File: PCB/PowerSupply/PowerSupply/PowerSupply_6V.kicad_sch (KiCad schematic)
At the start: 18 parts

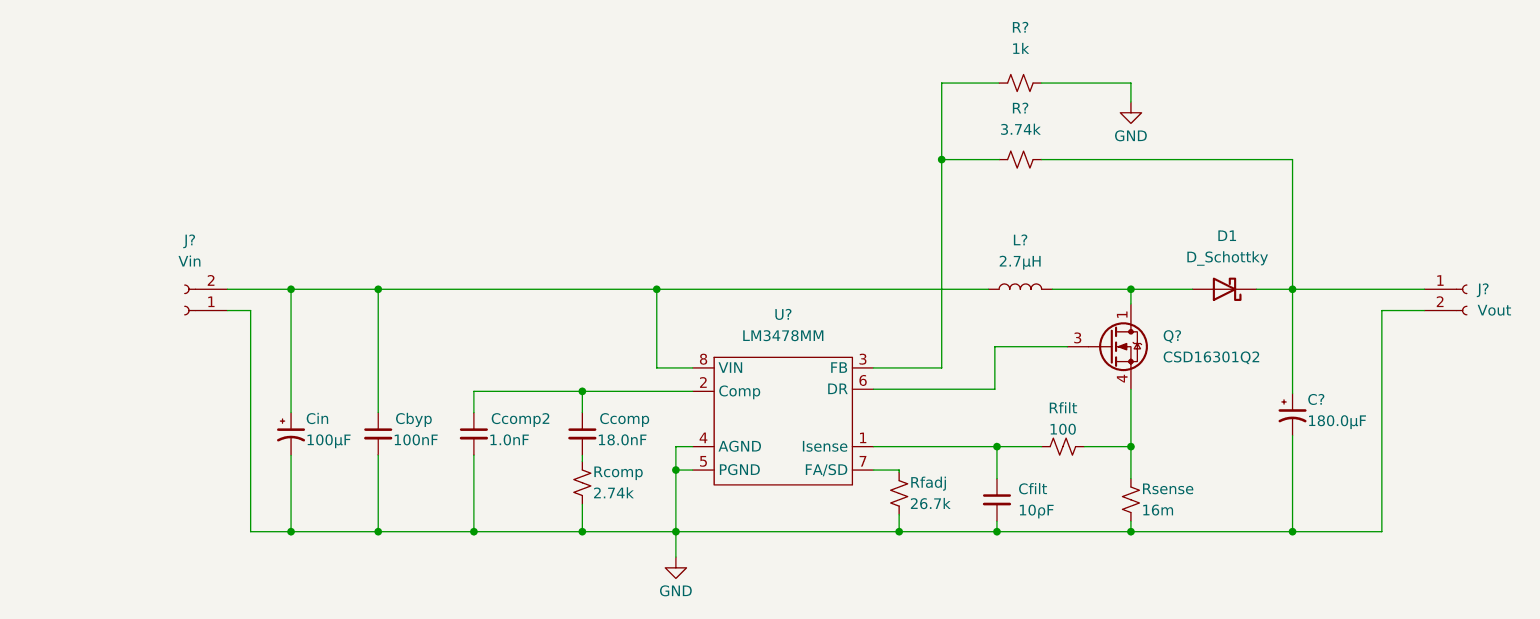
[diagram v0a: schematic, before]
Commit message: Finalized both power supply
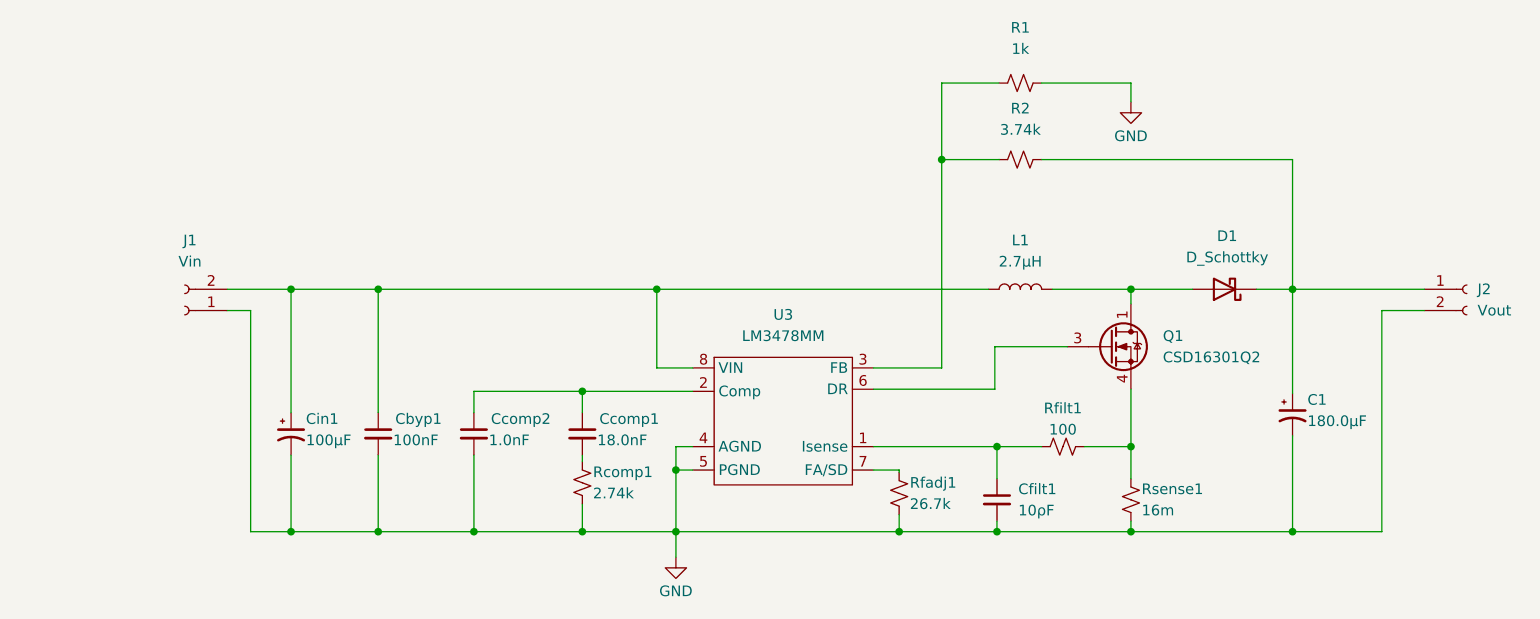
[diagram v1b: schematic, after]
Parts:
- gave numbers to parts that had none: 8
- renumbered Cbyp to Cbyp1, Ccomp to Ccomp1, Cfilt to Cfilt1, Cin to Cin1, Rcomp to Rcomp1, Rfadj to Rfadj1, Rfilt to Rfilt1, Rsense to Rsense1
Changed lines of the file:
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@@
   (symbol (lib_id "Device:L") (at 155.194 87.63 90) (unit 1)
     (in_bom yes) (on_board yes)
-    (property "Reference" "L?" (id 0) (at 155.194 81.788 90))
+    (property "Reference" "L1" (id 0) (at 155.194 81.788 90))
     (property "Value" "2.7µH" (id 1) (at 155.194 84.328 90))
     (property "Footprint" "Inductor_SMD:L_TDK_VLP8040" (id 2) (at 155.194 87.63 0)
@@
   (symbol (lib_id "Connector:Conn_01x02_Female") (at 55.372 90.17 180) (unit 1)
     (in_bom yes) (on_board yes) (fields_autoplaced)
-    (property "Reference" "J?" (id 0) (at 56.007 81.788 0))
+    (property "Reference" "J1" (id 0) (at 56.007 81.788 0))
     (property "Value" "Vin" (id 1) (at 56.007 84.328 0))
     (property "Footprint" "Connector_PinHeader_2.54mm:PinHeader_1x02_P2.54mm_Vertical" (id 2) (at 55.372 90.17 0)
@@
   (symbol (lib_id "Transistor_FET:CSD16301Q2") (at 165.862 94.488 0) (unit 1)
     (in_bom yes) (on_board yes) (fields_autoplaced)
-    (property "Reference" "Q?" (id 0) (at 172.212 93.2179 0)
+    (property "Reference" "Q1" (id 0) (at 172.212 93.2179 0)
       (effects (font (size 1.27 1.27)) (justify left))
     )
@@
   (symbol (lib_id "Device:C_Polarized_Small_US") (at 187.706 102.616 0) (unit 1)
     (in_bom yes) (on_board yes)
-    (property "Reference" "C?" (id 0) (at 189.484 100.838 0)
+    (property "Reference" "C1" (id 0) (at 189.484 100.838 0)
       (effects (font (size 1.27 1.27)) (justify left))
     )
@@
   (symbol (lib_id "Connector:Conn_01x02_Female") (at 208.534 87.63 0) (unit 1)
     (in_bom yes) (on_board yes) (fields_autoplaced)
-    (property "Reference" "J?" (id 0) (at 209.804 87.6299 0)
+    (property "Reference" "J2" (id 0) (at 209.804 87.6299 0)
       (effects (font (size 1.27 1.27)) (justify left))
     )
@@
   (symbol (lib_id "Device:R_Small_US") (at 155.194 72.136 90) (unit 1)
     (in_bom yes) (on_board yes) (fields_autoplaced)
-    (property "Reference" "R?" (id 0) (at 155.194 66.04 90))
+    (property "Reference" "R2" (id 0) (at 155.194 66.04 90))
     (property "Value" "3.74k" (id 1) (at 155.194 68.58 90))
     (property "Footprint" "Resistor_SMD:R_0402_1005Metric_Pad0.72x0.64mm_HandSolder" (id 2) (at 155.194 72.136 0)
@@
   (symbol (lib_id "Device:C_Polarized_Small_US") (at 68.072 104.902 0) (unit 1)
     (in_bom yes) (on_board yes)
-    (property "Reference" "Cin" (id 0) (at 69.85 103.124 0)
+    (property "Reference" "Cin1" (id 0) (at 69.85 103.124 0)
       (effects (font (size 1.27 1.27)) (justify left))
     )
@@
   (symbol (lib_id "Device:R_Small_US") (at 140.716 112.014 0) (unit 1)
     (in_bom yes) (on_board yes)
-    (property "Reference" "Rfadj" (id 0) (at 141.986 110.744 0)
+    (property "Reference" "Rfadj1" (id 0) (at 141.986 110.744 0)
       (effects (font (size 1.27 1.27)) (justify left))
     )
@@
   (symbol (lib_id "CustomPower:LM3478MM") (at 126.238 90.678 0) (unit 1)
     (in_bom yes) (on_board yes) (fields_autoplaced)
-    (property "Reference" "U?" (id 0) (at 126.873 90.678 0))
+    (property "Reference" "U3" (id 0) (at 126.873 90.678 0))
     (property "Value" "LM3478MM" (id 1) (at 126.873 93.218 0))
     (property "Footprint" "Package_SO:SOIC-8-1EP_3.9x4.9mm_P1.27mm_EP2.29x3mm" (id 2) (at 126.238 90.678 0)
@@
   (symbol (lib_id "Device:C_Small") (at 152.4 112.776 0) (unit 1)
     (in_bom yes) (on_board yes) (fields_autoplaced)
-    (property "Reference" "Cfilt" (id 0) (at 154.94 111.5122 0)
+    (property "Reference" "Cfilt1" (id 0) (at 154.94 111.5122 0)
       (effects (font (size 1.27 1.27)) (justify left))
     )
@@
   (symbol (lib_id "Device:R_Small_US") (at 155.194 62.992 90) (unit 1)
     (in_bom yes) (on_board yes) (fields_autoplaced)
-    (property "Reference" "R?" (id 0) (at 155.194 56.388 90))
+    (property "Reference" "R1" (id 0) (at 155.194 56.388 90))
     (property "Value" "1k" (id 1) (at 155.194 58.928 90))
     (property "Footprint" "Resistor_SMD:R_0402_1005Metric_Pad0.72x0.64mm_HandSolder" (id 2) (at 155.194 62.992 0)
@@
   (symbol (lib_id "power:GND") (at 114.046 119.634 0) (unit 1)
     (in_bom yes) (on_board yes)
-    (property "Reference" "#PWR?" (id 0) (at 114.046 125.984 0)
+    (property "Reference" "#PWR0101" (id 0) (at 114.046 125.984 0)
       (effects (font (size 1.27 1.27)) hide)
     )
@@
   (symbol (lib_id "Device:R_Small_US") (at 102.87 110.744 0) (unit 1)
     (in_bom yes) (on_board yes)
-    (property "Reference" "Rcomp" (id 0) (at 104.14 109.474 0)
+    (property "Reference" "Rcomp1" (id 0) (at 104.14 109.474 0)
       (effects (font (size 1.27 1.27)) (justify left))
     )
@@
   (symbol (lib_id "Device:C_Small") (at 78.486 104.902 0) (unit 1)
     (in_bom yes) (on_board yes)
-    (property "Reference" "Cbyp" (id 0) (at 80.518 103.124 0)
+    (property "Reference" "Cbyp1" (id 0) (at 80.518 103.124 0)
       (effects (font (size 1.27 1.27)) (justify left))
     )
@@
   (symbol (lib_id "Device:C_Small") (at 102.87 104.902 0) (unit 1)
     (in_bom yes) (on_board yes)
-    (property "Reference" "Ccomp" (id 0) (at 104.902 103.124 0)
+    (property "Reference" "Ccomp1" (id 0) (at 104.902 103.124 0)
       (effects (font (size 1.27 1.27)) (justify left))
     )
@@
   (symbol (lib_id "Device:R_Small_US") (at 160.274 106.426 90) (unit 1)
     (in_bom yes) (on_board yes)
-    (property "Reference" "Rfilt" (id 0) (at 160.274 101.854 90))
+    (property "Reference" "Rfilt1" (id 0) (at 160.274 101.854 90))
     (property "Value" "100" (id 1) (at 160.274 104.394 90))
     (property "Footprint" "Resistor_SMD:R_0805_2012Metric_Pad1.20x1.40mm_HandSolder" (id 2) (at 160.274 106.426 0)
@@
   (symbol (lib_id "Device:R_Small_US") (at 168.402 112.776 0) (unit 1)
     (in_bom yes) (on_board yes)
-    (property "Reference" "Rsense" (id 0) (at 169.672 111.506 0)
+    (property "Reference" "Rsense1" (id 0) (at 169.672 111.506 0)
       (effects (font (size 1.27 1.27)) (justify left))
     )
@@
   (symbol (lib_id "power:GND") (at 168.402 65.278 0) (unit 1)
     (in_bom yes) (on_board yes)
-    (property "Reference" "#PWR?" (id 0) (at 168.402 71.628 0)
-      (effects (font (size 1.27 1.27)) hide)
-    )
+    (property "Reference" "#PWR0102" (id 0) (at 168.402 71.628 0)
+      (effects (font (size 1.27 1.27)) hide)
+    )

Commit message: Fixed Zach's errors :/ smh
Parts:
- added J6: Vout, Connector_PinHeader_2.54mm:PinHeader_1x02_P2.54mm_Vertical, symbol Connector:Conn_01x02_Female
- Cbyp1: footprint Capacitor_SMD:C_0402_1005Metric_Pad0.74x0.62mm_HandSolder -> Capacitor_SMD:C_0805_2012Metric_Pad1.18x1.45mm_HandSolder
- Ccomp1, R1, R2, Rfadj1: footprint Resistor_SMD:R_0402_1005Metric_Pad0.72x0.64mm_HandSolder -> Resistor_SMD:R_0805_2012Metric_Pad1.20x1.40mm_HandSolder
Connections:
- net GND: now also J6.2 (Pin_2)
- net at C1.1, D1.1 (K), J2.1 (Pin_1)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: now also J6.1 (Pin_1)
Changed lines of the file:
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@@
   (junction (at 102.87 99.822) (diameter 0) (color 0 0 0 0)
   )
+  (junction (at 187.706 93.98) (diameter 0) (color 0 0 0 0)
+  )
   (junction (at 145.796 72.136) (diameter 0) (color 0 0 0 0)
   )
@@
   (junction (at 187.706 87.63) (diameter 0) (color 0 0 0 0)
   )
+  (junction (at 198.374 96.52) (diameter 0) (color 0 0 0 0)
+  )
   (junction (at 168.402 106.426) (diameter 0) (color 0 0 0 0)
   )
@@
     (stroke (width 0) (type default) (color 0 0 0 0))
   )
+  (wire (pts (xy 198.374 96.52) (xy 198.374 116.586))
+    (stroke (width 0) (type default) (color 0 0 0 0))
+  )
   (wire (pts (xy 114.046 116.586) (xy 140.716 116.586))
     (stroke (width 0) (type default) (color 0 0 0 0))
@@
     (stroke (width 0) (type default) (color 0 0 0 0))
   )
+  (wire (pts (xy 187.706 93.98) (xy 203.454 93.98))
+    (stroke (width 0) (type default) (color 0 0 0 0))
+  )
   (wire (pts (xy 78.486 116.586) (xy 89.916 116.586))
     (stroke (width 0) (type default) (color 0 0 0 0))
@@
     (stroke (width 0) (type default) (color 0 0 0 0))
   )
-  (wire (pts (xy 187.706 87.63) (xy 187.706 100.076))
+  (wire (pts (xy 187.706 87.63) (xy 187.706 93.98))
     (stroke (width 0) (type default) (color 0 0 0 0))
   )
@@
     (stroke (width 0) (type default) (color 0 0 0 0))
   )
+  (wire (pts (xy 198.374 96.52) (xy 203.454 96.52))
+    (stroke (width 0) (type default) (color 0 0 0 0))
+  )
   (wire (pts (xy 89.916 99.822) (xy 102.87 99.822))
     (stroke (width 0) (type default) (color 0 0 0 0))
@@
     (stroke (width 0) (type default) (color 0 0 0 0))
   )
-  (wire (pts (xy 198.374 90.17) (xy 198.374 116.586))
+  (wire (pts (xy 198.374 90.17) (xy 198.374 96.52))
+    (stroke (width 0) (type default) (color 0 0 0 0))
+  )
+  (wire (pts (xy 187.706 93.98) (xy 187.706 100.076))
     (stroke (width 0) (type default) (color 0 0 0 0))
   )
@@
     (property "Reference" "R2" (id 0) (at 155.194 66.04 90))
     (property "Value" "3.74k" (id 1) (at 155.194 68.58 90))
-    (property "Footprint" "Resistor_SMD:R_0402_1005Metric_Pad0.72x0.64mm_HandSolder" (id 2) (at 155.194 72.136 0)
+    (property "Footprint" "Resistor_SMD:R_0805_2012Metric_Pad1.20x1.40mm_HandSolder" (id 2) (at 155.194 72.136 0)
       (effects (font (size 1.27 1.27)) hide)
     )
@@
       (effects (font (size 1.27 1.27)) (justify left))
     )
-    (property "Footprint" "Resistor_SMD:R_0402_1005Metric_Pad0.72x0.64mm_HandSolder" (id 2) (at 140.716 112.014 0)
+    (property "Footprint" "Resistor_SMD:R_0805_2012Metric_Pad1.20x1.40mm_HandSolder" (id 2) (at 140.716 112.014 0)
       (effects (font (size 1.27 1.27)) hide)
     )
@@
     (property "Reference" "R1" (id 0) (at 155.194 56.388 90))
     (property "Value" "1k" (id 1) (at 155.194 58.928 90))
-    (property "Footprint" "Resistor_SMD:R_0402_1005Metric_Pad0.72x0.64mm_HandSolder" (id 2) (at 155.194 62.992 0)
+    (property "Footprint" "Resistor_SMD:R_0805_2012Metric_Pad1.20x1.40mm_HandSolder" (id 2) (at 155.194 62.992 0)
       (effects (font (size 1.27 1.27)) hide)
     )
     (property "Datasheet" "~" (id 3) (at 155.194 62.992 0)
+      (effects (font (size 1.27 1.27)) hide)
+    )
+    (pin "1")
+    (pin "2")
+  )
+  (symbol (lib_id "Connector:Conn_01x02_Female") (at 208.534 93.98 0) (unit 1)
+    (in_bom yes) (on_board yes) (fields_autoplaced)
+    (property "Reference" "J6" (id 0) (at 209.804 93.9799 0)
+      (effects (font (size 1.27 1.27)) (justify left))
+    )
+    (property "Value" "Vout" (id 1) (at 209.804 96.5199 0)
+      (effects (font (size 1.27 1.27)) (justify left))
+    )
+    (property "Footprint" "Connector_PinHeader_2.54mm:PinHeader_1x02_P2.54mm_Vertical" (id 2) (at 208.534 93.98 0)
+      (effects (font (size 1.27 1.27)) hide)
+    )
+    (property "Datasheet" "~" (id 3) (at 208.534 93.98 0)
       (effects (font (size 1.27 1.27)) hide)
     )
@@
       (effects (font (size 1.27 1.27)) (justify left))
     )
-    (property "Footprint" "Capacitor_SMD:C_0402_1005Metric_Pad0.74x0.62mm_HandSolder" (id 2) (at 78.486 104.902 0)
+    (property "Footprint" "Capacitor_SMD:C_0805_2012Metric_Pad1.18x1.45mm_HandSolder" (id 2) (at 78.486 104.902 0)
       (effects (font (size 1.27 1.27)) hide)
     )
@@
       (effects (font (size 1.27 1.27)) (justify left))
     )
-    (property "Footprint" "Resistor_SMD:R_0402_1005Metric_Pad0.72x0.64mm_HandSolder" (id 2) (at 102.87 104.902 0)
-      (effects (font (size 1.27 1.27)) hide)
-    )
+    (property "Footprint" "Resistor_SMD:R_0805_2012Metric_Pad1.20x1.40mm_HandSolder" (id 2) (at 102.87 104.902 0)
+      (effects (font (size 1.27 1.27)) hide)
+    )

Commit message: Finished v0.1
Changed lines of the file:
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@@
+    (stroke (width 0) (type default) (color 0 0 0 0))
+  )
+  (wire (pts (xy 40.894 113.792) (xy 40.894 116.84))
     (stroke (width 0) (type default) (color 0 0 0 0))
   )
@@
     (pin "2")
   )
+  (symbol (lib_id "power:PWR_FLAG") (at 40.894 113.792 0) (unit 1)
+    (in_bom yes) (on_board yes) (fields_autoplaced)
+    (property "Reference" "#FLG0101" (id 0) (at 40.894 111.887 0)
+      (effects (font (size 1.27 1.27)) hide)
+    )
+    (property "Value" "PWR_FLAG" (id 1) (at 40.894 109.22 0))
+    (property "Footprint" "" (id 2) (at 40.894 113.792 0)
+      (effects (font (size 1.27 1.27)) hide)
+    )
+    (property "Datasheet" "~" (id 3) (at 40.894 113.792 0)
+      (effects (font (size 1.27 1.27)) hide)
+    )
+    (pin "1")
+  )
   (symbol (lib_id "Device:R_Small_US") (at 140.716 112.014 0) (unit 1)
     (in_bom yes) (on_board yes)
@@
     (pin "2")
   )
+  (symbol (lib_id "power:GND") (at 40.894 116.84 0) (unit 1)
+    (in_bom yes) (on_board yes)
+    (property "Reference" "#PWR0105" (id 0) (at 40.894 123.19 0)
+      (effects (font (size 1.27 1.27)) hide)
+    )
+    (property "Value" "GND" (id 1) (at 40.894 120.904 0))
+    (property "Footprint" "" (id 2) (at 40.894 116.84 0)
+      (effects (font (size 1.27 1.27)) hide)
+    )
+    (property "Datasheet" "" (id 3) (at 40.894 116.84 0)
+      (effects (font (size 1.27 1.27)) hide)
+    )
+    (pin "1")
+  )
 )
